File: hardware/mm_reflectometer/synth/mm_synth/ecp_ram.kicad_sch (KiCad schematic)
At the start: 8 parts, among them J1701 Conn_Coaxial, J1702 Conn_Coaxial, U1601 ECP5U_25_CABGA256, U1701 IS66WVH16M8ALL

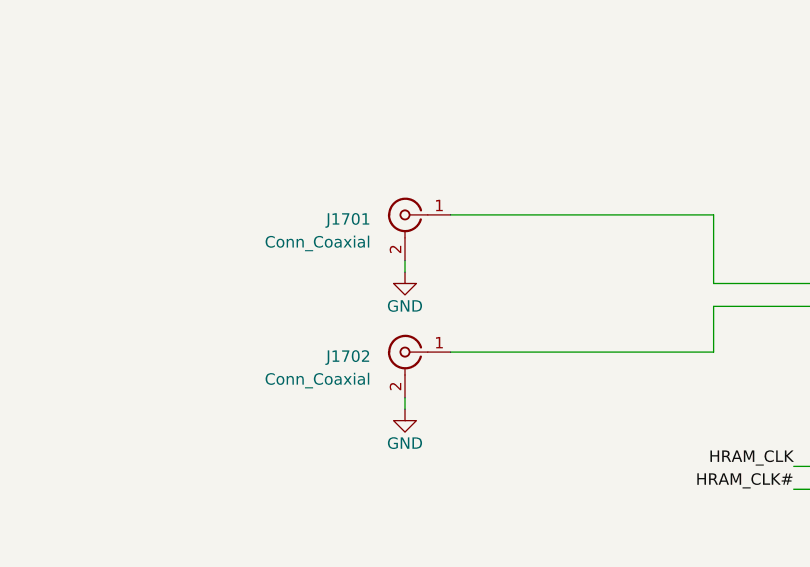
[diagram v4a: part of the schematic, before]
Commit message: more component placement on mm synth
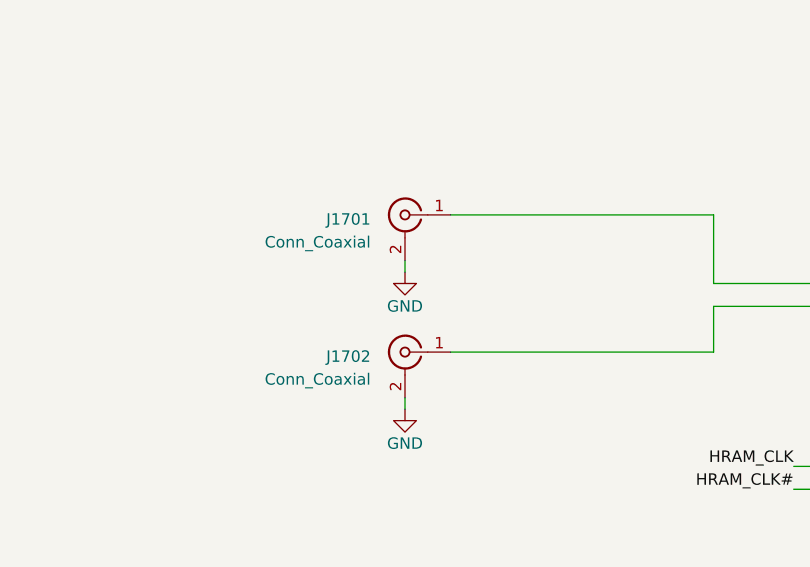
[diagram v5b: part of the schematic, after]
